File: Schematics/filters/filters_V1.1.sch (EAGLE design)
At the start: 110 parts, among them IC1 NE5532N, IC2 NE5532N, IC3 NE5532N, IC4 NE5532N, IC5 NE5532N, IC6 NE5532N, IC7 NE5532N, J1 3_PIN_AMPCONN, J2 3_PIN_AMPCONN, J3 3_PIN_AMPCONN

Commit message: final board update before order
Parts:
- J2: value 3_PIN_AMPCONN -> 4_PIN_AMPCONN; device Amplifier_Parts:3_PIN_AMPCONN -> Amplifier_Parts:4_PIN_AMPCONN
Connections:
- net GND: now also J2.4, VR2G$1.TAB, VR2G$2.TAB, VR3G$1.TAB, VR3G$2.TAB, VR4G$1.TAB, VR4G$2.TAB
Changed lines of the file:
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@@
 <setting verticaltext="up"/>
 </settings>
-<grid distance="0.1" unitdist="inch" unit="inch" style="lines" multiple="1" display="no" altdistance="0.01" altunitdist="inch" altunit="inch"/>
+<grid distance="0.1" unitdist="inch" unit="inch" style="lines" multiple="1" display="yes" altdistance="0.01" altunitdist="inch" altunit="inch"/>
 <layers>
 <layer number="1" name="Top" color="4" fill="1" visible="no" active="no"/>
@@
 <part name="VR4" library="Amplifier_Parts" deviceset="P140KV1-F25BR" device="" value="10k"/>
 <part name="J1" library="Amplifier_Parts" deviceset="3_PIN_AMPCONN" device=""/>
-<part name="J2" library="Amplifier_Parts" deviceset="3_PIN_AMPCONN" device=""/>
 <part name="J3" library="Amplifier_Parts" deviceset="3_PIN_AMPCONN" device=""/>
 <part name="IC1" library="linear" deviceset="NE5532" device="N"/>
@@
 <part name="R48" library="rcl" deviceset="R-US_" device="0204/2V" value="4.7k"/>
 <part name="R49" library="rcl" deviceset="R-US_" device="0204/2V" value="4.7k"/>
+<part name="GND23" library="supply2" deviceset="GND" device=""/>
+<part name="GND24" library="supply2" deviceset="GND" device=""/>
+<part name="GND25" library="supply2" deviceset="GND" device=""/>
+<part name="J2" library="Amplifier_Parts" deviceset="4_PIN_AMPCONN" device=""/>
+<part name="GND27" library="supply2" deviceset="GND" device=""/>
 </parts>
 <sheets>
@@
 <instance part="VR4" gate="B" x="317.5" y="175.26"/>
 <instance part="J1" gate="G$1" x="93.98" y="195.58"/>
-<instance part="J2" gate="G$1" x="482.6" y="180.34" rot="MR0"/>
 <instance part="J3" gate="G$1" x="73.66" y="347.98"/>
 <instance part="IC1" gate="A" x="154.94" y="243.84" rot="MR180"/>
@@
 <instance part="R48" gate="G$1" x="312.42" y="111.76" rot="R90"/>
 <instance part="R49" gate="G$1" x="312.42" y="68.58" rot="R90"/>
+<instance part="VR2" gate="G$1" x="342.9" y="398.78" rot="R180"/>
+<instance part="VR2" gate="G$2" x="345.44" y="398.78" rot="R180"/>
+<instance part="VR3" gate="G$1" x="350.52" y="398.78" rot="R180"/>
+<instance part="VR3" gate="G$2" x="353.06" y="398.78" rot="R180"/>
+<instance part="VR4" gate="G$1" x="358.14" y="398.78" rot="R180"/>
+<instance part="VR4" gate="G$2" x="360.68" y="398.78" rot="R180"/>
+<instance part="GND23" gate="GND" x="342.9" y="393.7"/>
+<instance part="GND24" gate="GND" x="350.52" y="393.7"/>
+<instance part="GND25" gate="GND" x="358.14" y="393.7"/>
+<instance part="J2" gate="G$1" x="482.6" y="180.34" rot="MR0"/>
+<instance part="GND27" gate="GND" x="474.98" y="170.18"/>
 </instances>
 <busses>
@@
 <pinref part="GND6" gate="GND" pin="GND"/>
 <pinref part="R49" gate="G$1" pin="1"/>
+</segment>
+<segment>
+<pinref part="VR2" gate="G$1" pin="TAB"/>
+<pinref part="VR2" gate="G$2" pin="TAB"/>
+<wire x1="342.9" y1="398.78" x2="345.44" y2="398.78" width="0.1524" layer="91"/>
+<pinref part="GND23" gate="GND" pin="GND"/>
+<wire x1="342.9" y1="398.78" x2="342.9" y2="396.24" width="0.1524" layer="91"/>
+<junction x="342.9" y="398.78"/>
+</segment>
+<segment>
+<pinref part="GND24" gate="GND" pin="GND"/>
+<pinref part="VR3" gate="G$1" pin="TAB"/>
+<wire x1="350.52" y1="396.24" x2="350.52" y2="398.78" width="0.1524" layer="91"/>
+<pinref part="VR3" gate="G$2" pin="TAB"/>
+<wire x1="350.52" y1="398.78" x2="353.06" y2="398.78" width="0.1524" layer="91"/>
+<junction x="350.52" y="398.78"/>
+</segment>
+<segment>
+<pinref part="GND25" gate="GND" pin="GND"/>
+<pinref part="VR4" gate="G$1" pin="TAB"/>
+<wire x1="358.14" y1="396.24" x2="358.14" y2="398.78" width="0.1524" layer="91"/>
+<pinref part="VR4" gate="G$2" pin="TAB"/>
+<wire x1="358.14" y1="398.78" x2="360.68" y2="398.78" width="0.1524" layer="91"/>
+<junction x="358.14" y="398.78"/>
+</segment>
+<segment>
+<pinref part="GND27" gate="GND" pin="GND"/>
+<wire x1="474.98" y1="172.72" x2="474.98" y2="175.26" width="0.1524" layer="91"/>
+<pinref part="J2" gate="G$1" pin="4"/>
+<wire x1="474.98" y1="175.26" x2="477.52" y2="175.26" width="0.1524" layer="91"/>
 </segment>
 </net>
@@
 <wire x1="365.76" y1="246.38" x2="414.02" y2="246.38" width="0.1524" layer="91"/>
 <wire x1="414.02" y1="246.38" x2="414.02" y2="182.88" width="0.1524" layer="91"/>
+<wire x1="414.02" y1="182.88" x2="477.52" y2="182.88" width="0.1524" layer="91"/>
 <pinref part="J2" gate="G$1" pin="1"/>
-<wire x1="414.02" y1="182.88" x2="477.52" y2="182.88" width="0.1524" layer="91"/>
-</segment>
-</net>
+</segment>
+</net>

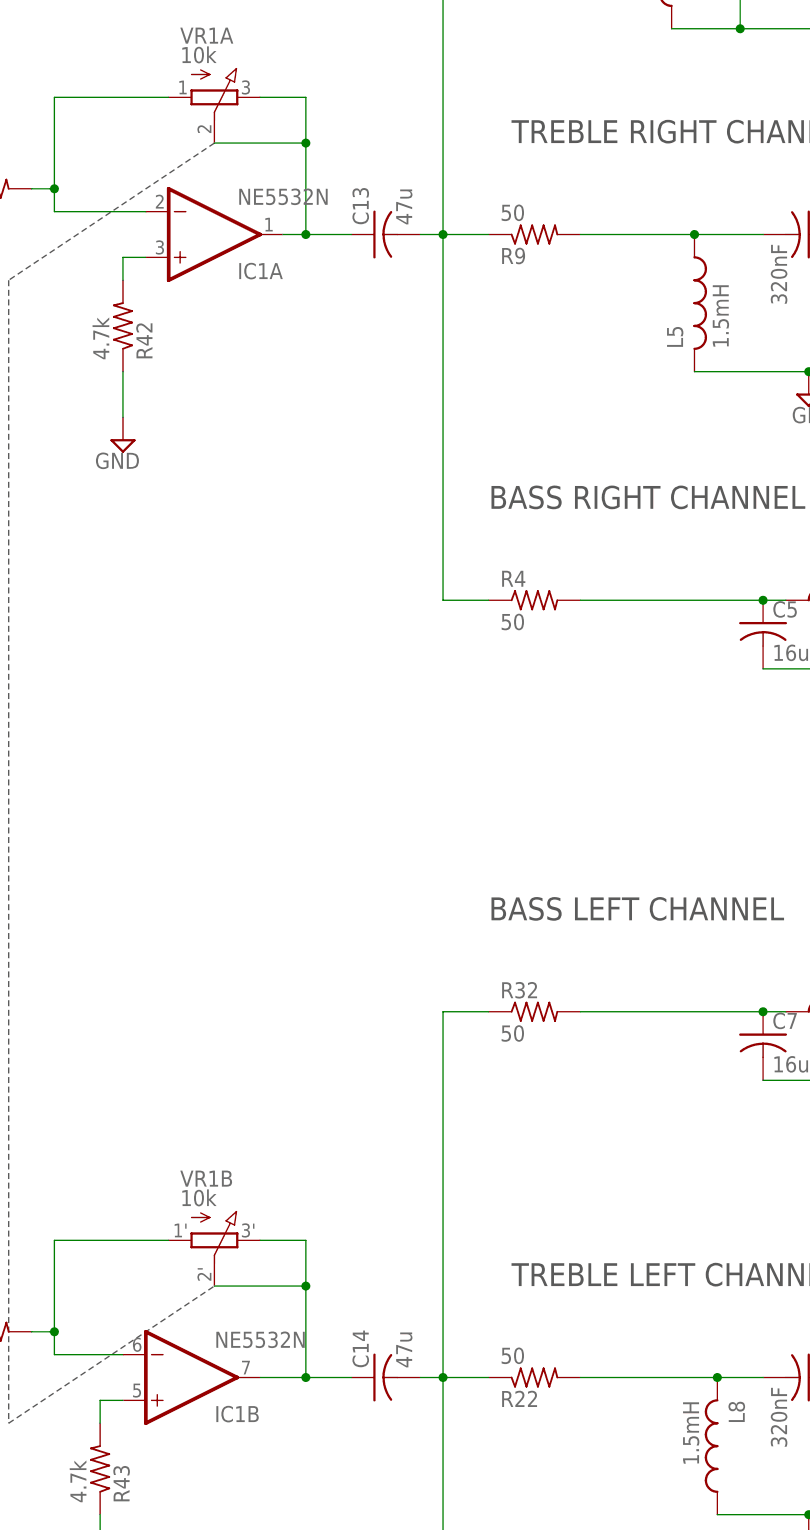
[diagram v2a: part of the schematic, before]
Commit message: fixed the stupid mistake on the pot
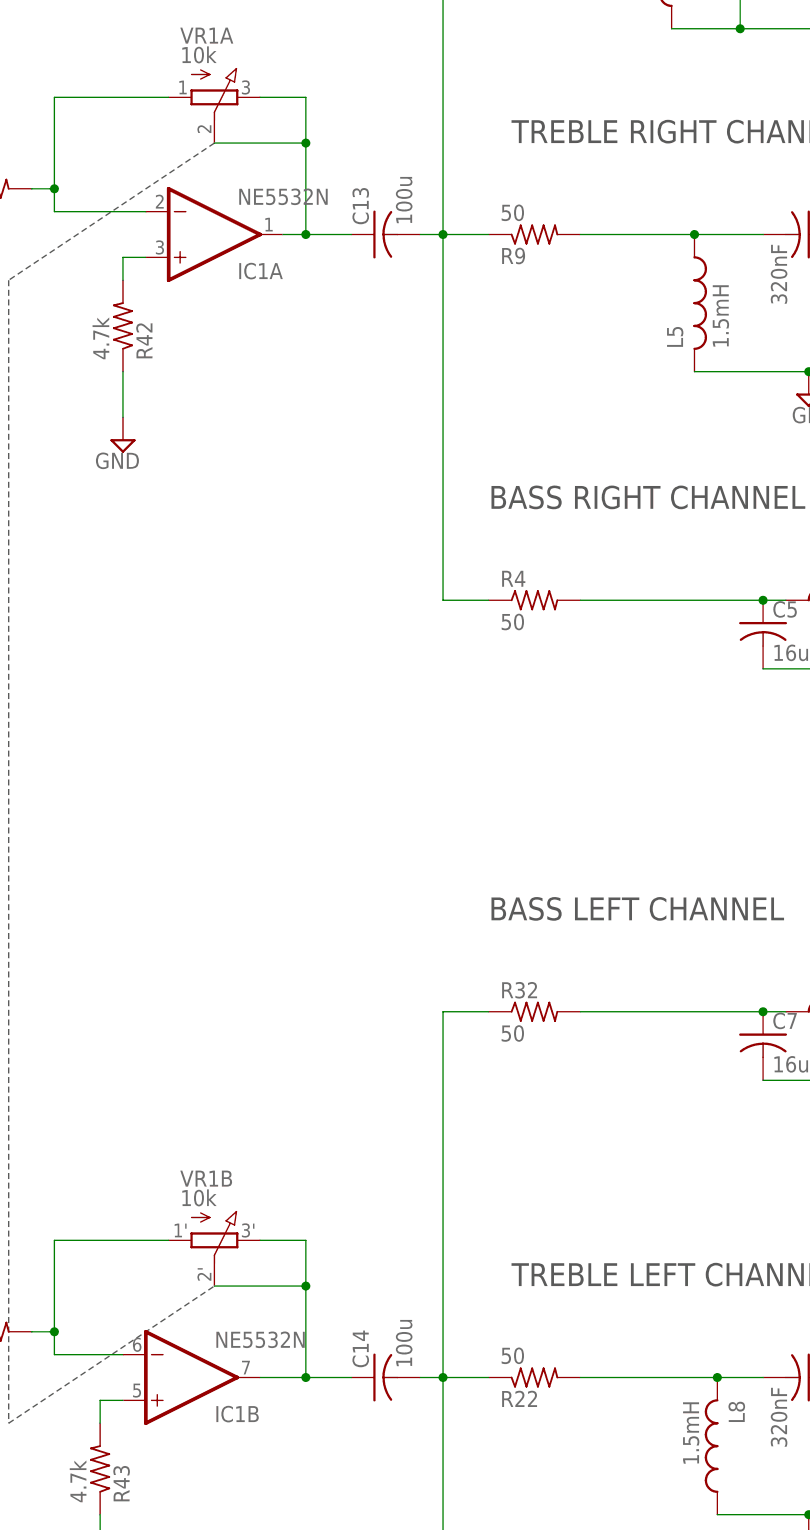
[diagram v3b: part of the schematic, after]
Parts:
- C13, C14: value 47u -> 100u
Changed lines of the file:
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@@
 <?xml version="1.0" encoding="utf-8"?>
 <!DOCTYPE eagle SYSTEM "eagle.dtd">
-<eagle version="6.5.0">
+<eagle version="7.4.0">
 <drawing>
 <settings>
@@
 <part name="C11" library="rcl" deviceset="C-US" device="050-024X044" value="660nF"/>
 <part name="C12" library="rcl" deviceset="C-US" device="050-024X044" value="660nF"/>
-<part name="C13" library="rcl" deviceset="C-US" device="050-024X044" value="47u"/>
-<part name="C14" library="rcl" deviceset="C-US" device="050-024X044" value="47u"/>
+<part name="C13" library="rcl" deviceset="C-US" device="050-024X044" value="100u"/>
+<part name="C14" library="rcl" deviceset="C-US" device="050-024X044" value="100u"/>
 <part name="GND22" library="supply2" deviceset="GND" device=""/>
 <part name="VR1" library="Amplifier_Parts" deviceset="VOL_POT_2GANG" device="" value="10k"/>

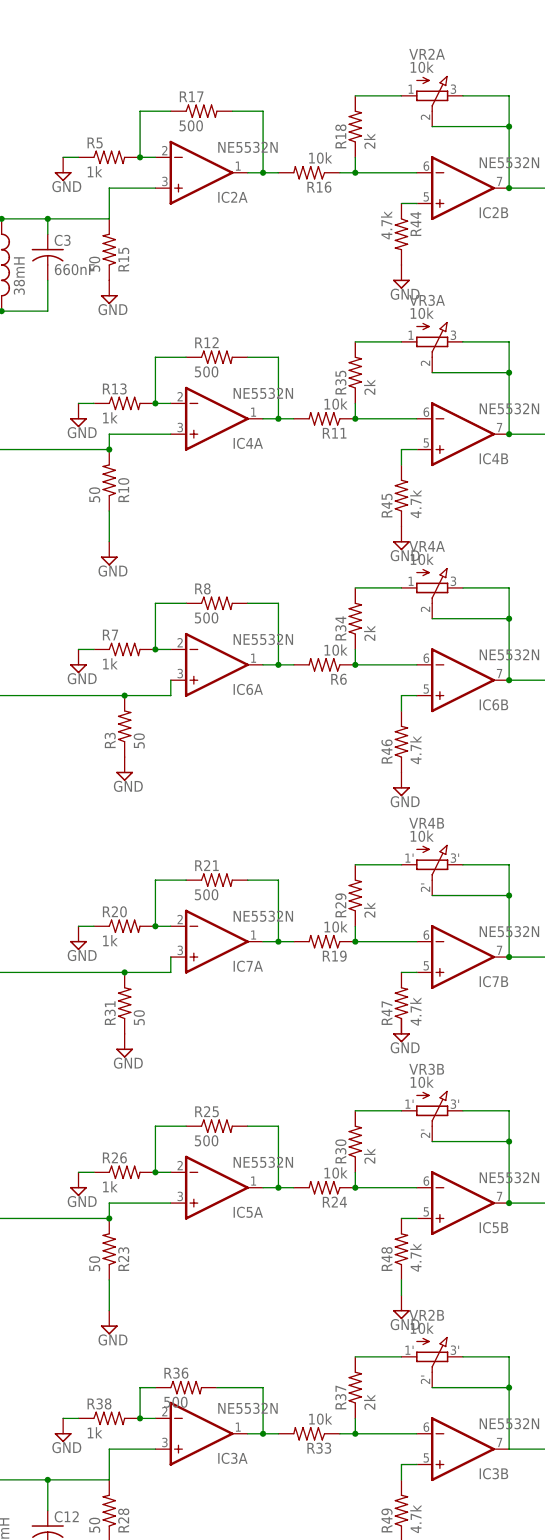
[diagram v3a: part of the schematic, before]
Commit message: now all the filter board fixes are there
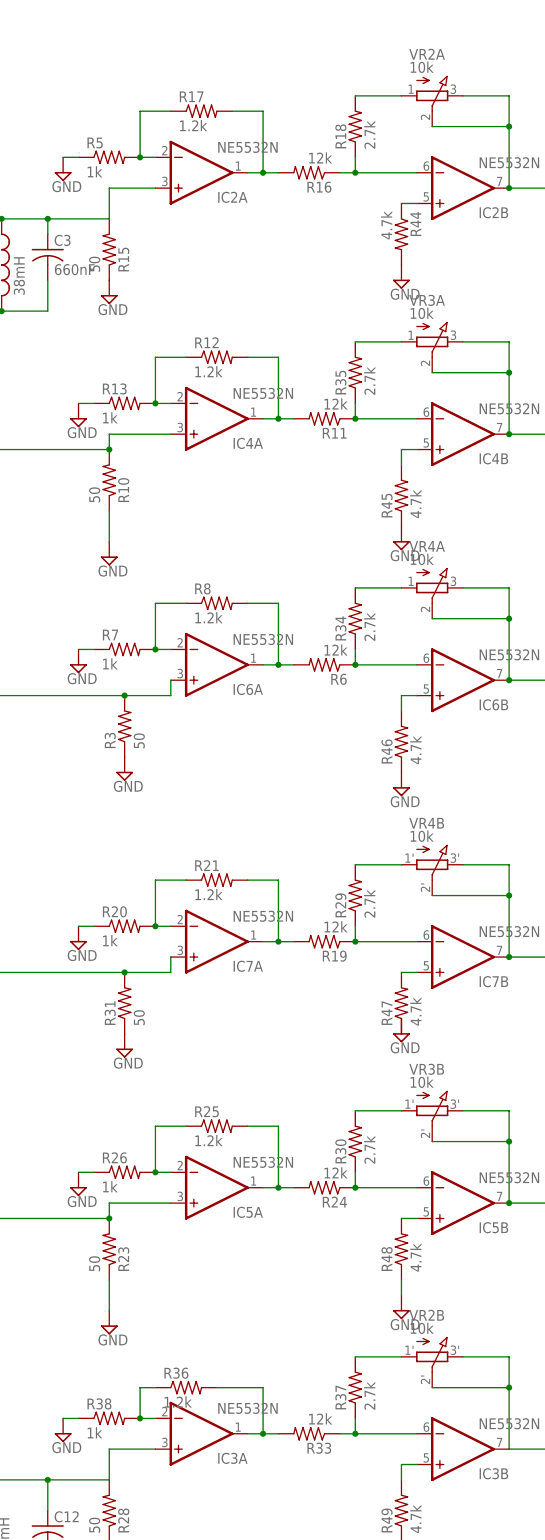
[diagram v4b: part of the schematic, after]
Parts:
- R11, R16, R19, R24, R33, R6: value 10k -> 12k
- R12, R17, R21, R25, R36, R8: value 500 -> 1.2k
- R18, R29, R30, R34, R35, R37: value 2k -> 2.7k
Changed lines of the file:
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@@
 <parts>
 <part name="C1" library="rcl" deviceset="C-US" device="050-024X044" value="7.4uF"/>
-<part name="R6" library="rcl" deviceset="R-US_" device="0204/2V" value="10k"/>
+<part name="R6" library="rcl" deviceset="R-US_" device="0204/2V" value="12k"/>
 <part name="R7" library="rcl" deviceset="R-US_" device="0204/2V" value="1k"/>
-<part name="R8" library="rcl" deviceset="R-US_" device="0204/2V" value="500"/>
+<part name="R8" library="rcl" deviceset="R-US_" device="0204/2V" value="1.2k"/>
 <part name="R9" library="rcl" deviceset="R-US_" device="0204/2V" value="50"/>
 <part name="R10" library="rcl" deviceset="R-US_" device="0204/2V" value="50"/>
-<part name="R11" library="rcl" deviceset="R-US_" device="0204/2V" value="10k"/>
-<part name="R12" library="rcl" deviceset="R-US_" device="0204/2V" value="500"/>
+<part name="R11" library="rcl" deviceset="R-US_" device="0204/2V" value="12k"/>
+<part name="R12" library="rcl" deviceset="R-US_" device="0204/2V" value="1.2k"/>
 <part name="R13" library="rcl" deviceset="R-US_" device="0204/2V" value="1k"/>
 <part name="R14" library="rcl" deviceset="R-US_" device="0204/2V" value="50"/>
 <part name="R15" library="rcl" deviceset="R-US_" device="0204/2V" value="50"/>
-<part name="R34" library="rcl" deviceset="R-US_" device="0204/2V" value="2k"/>
-<part name="R35" library="rcl" deviceset="R-US_" device="0204/2V" value="2k"/>
+<part name="R34" library="rcl" deviceset="R-US_" device="0204/2V" value="2.7k"/>
+<part name="R35" library="rcl" deviceset="R-US_" device="0204/2V" value="2.7k"/>
 <part name="R3" library="rcl" deviceset="R-US_" device="0204/2V" value="50"/>
 <part name="R4" library="rcl" deviceset="R-US_" device="0204/2V" value="50"/>
-<part name="R16" library="rcl" deviceset="R-US_" device="0204/2V" value="10k"/>
-<part name="R17" library="rcl" deviceset="R-US_" device="0204/2V" value="500"/>
-<part name="R18" library="rcl" deviceset="R-US_" device="0204/2V" value="2k"/>
+<part name="R16" library="rcl" deviceset="R-US_" device="0204/2V" value="12k"/>
+<part name="R17" library="rcl" deviceset="R-US_" device="0204/2V" value="1.2k"/>
+<part name="R18" library="rcl" deviceset="R-US_" device="0204/2V" value="2.7k"/>
 <part name="R5" library="rcl" deviceset="R-US_" device="0204/2V" value="1k"/>
 <part name="C29" library="rcl" deviceset="C-US" device="050-024X044" value="0.1uF"/>
@@
 <part name="GND57" library="supply2" deviceset="GND" device=""/>
 <part name="GND58" library="supply2" deviceset="GND" device=""/>
-<part name="R19" library="rcl" deviceset="R-US_" device="0204/2V" value="10k"/>
+<part name="R19" library="rcl" deviceset="R-US_" device="0204/2V" value="12k"/>
 <part name="R20" library="rcl" deviceset="R-US_" device="0204/2V" value="1k"/>
-<part name="R21" library="rcl" deviceset="R-US_" device="0204/2V" value="500"/>
+<part name="R21" library="rcl" deviceset="R-US_" device="0204/2V" value="1.2k"/>
 <part name="R22" library="rcl" deviceset="R-US_" device="0204/2V" value="50"/>
 <part name="R23" library="rcl" deviceset="R-US_" device="0204/2V" value="50"/>
-<part name="R24" library="rcl" deviceset="R-US_" device="0204/2V" value="10k"/>
-<part name="R25" library="rcl" deviceset="R-US_" device="0204/2V" value="500"/>
+<part name="R24" library="rcl" deviceset="R-US_" device="0204/2V" value="12k"/>
+<part name="R25" library="rcl" deviceset="R-US_" device="0204/2V" value="1.2k"/>
 <part name="R26" library="rcl" deviceset="R-US_" device="0204/2V" value="1k"/>
 <part name="R27" library="rcl" deviceset="R-US_" device="0204/2V" value="50"/>
 <part name="R28" library="rcl" deviceset="R-US_" device="0204/2V" value="50"/>
-<part name="R29" library="rcl" deviceset="R-US_" device="0204/2V" value="2k"/>
-<part name="R30" library="rcl" deviceset="R-US_" device="0204/2V" value="2k"/>
+<part name="R29" library="rcl" deviceset="R-US_" device="0204/2V" value="2.7k"/>
+<part name="R30" library="rcl" deviceset="R-US_" device="0204/2V" value="2.7k"/>
 <part name="R31" library="rcl" deviceset="R-US_" device="0204/2V" value="50"/>
 <part name="R32" library="rcl" deviceset="R-US_" device="0204/2V" value="50"/>
-<part name="R33" library="rcl" deviceset="R-US_" device="0204/2V" value="10k"/>
-<part name="R36" library="rcl" deviceset="R-US_" device="0204/2V" value="500"/>
-<part name="R37" library="rcl" deviceset="R-US_" device="0204/2V" value="2k"/>
+<part name="R33" library="rcl" deviceset="R-US_" device="0204/2V" value="12k"/>
+<part name="R36" library="rcl" deviceset="R-US_" device="0204/2V" value="1.2k"/>
+<part name="R37" library="rcl" deviceset="R-US_" device="0204/2V" value="2.7k"/>
 <part name="R38" library="rcl" deviceset="R-US_" device="0204/2V" value="1k"/>
 <part name="GND4" library="supply2" deviceset="GND" device=""/>
